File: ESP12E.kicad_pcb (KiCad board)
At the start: 2 copper layers, 40.6 x 41.5 mm, 32 parts, among them J1 Conn_01x06_Pin, J2 Conn_01x06_Pin, P1 USB_C_Plug_USB2.0, Q3 SS8050, Q4 SS8050, U1 ESP-12E, U2 CH340G, U3 AMS1117-3.3, Y1 Crystal_GND23

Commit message: Feat: adding IRF520 mosfets for controlling Motor of air pump and 4 solinoids.
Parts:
- removed C5: 10pF, Capacitor_SMD:C_0201_0603Metric
- removed C6: 10uF, Capacitor_SMD:C_0201_0603Metric
- removed C7: 100nF, Capacitor_SMD:C_0201_0603Metric
- removed P1: USB_C_Plug_USB2.0, Connector_USB:USB_C_Receptacle_GCT_USB4125-xx-x_6P_TopMnt_Horizontal
- removed U2: CH340G, Package_SO:SOIC-16_3.9x9.9mm_P1.27mm
- removed Y1: Crystal_GND23, Crystal:Crystal_SMD_3225-4Pin_3.2x2.5mm
- added D2: LED, LED_SMD:LED_1206_3216Metric, F.Cu at (54.8, 101.0)
- added D3: LED, LED_SMD:LED_1206_3216Metric, F.Cu at (67.8, 101.0)
- added D4: LED, LED_SMD:LED_1206_3216Metric, F.Cu at (80.8, 101.0)
- added D5: LED, LED_SMD:LED_1206_3216Metric, F.Cu at (93.8, 101.0)
- added J3: UART, Connector_JST:JST_XH_B4B-XH-A_1x04_P2.50mm_Vertical, F.Cu at (28.5, 36.2)
- added J4: Motor, TerminalBlock_Phoenix:TerminalBlock_Phoenix_PT-1,5-2-5.0-H_1x02_P5.00mm_Horizontal, F.Cu at (35.0, 113.0)
- added J5: 12v PWR, TerminalBlock_Phoenix:TerminalBlock_Phoenix_PT-1,5-2-5.0-H_1x02_P5.00mm_Horizontal, F.Cu at (110.5, 113.0)
- added J6: Sol_1, TerminalBlock_Phoenix:TerminalBlock_Phoenix_PT-1,5-2-5.0-H_1x02_P5.00mm_Horizontal, F.Cu at (48.0, 113.0)
- added J7: Sol_2, TerminalBlock_Phoenix:TerminalBlock_Phoenix_PT-1,5-2-5.0-H_1x02_P5.00mm_Horizontal, F.Cu at (61.0, 113.0)
- added J8: Sol_3, TerminalBlock_Phoenix:TerminalBlock_Phoenix_PT-1,5-2-5.0-H_1x02_P5.00mm_Horizontal, F.Cu at (74.0, 113.0)
- added J9: Sol_4, TerminalBlock_Phoenix:TerminalBlock_Phoenix_PT-1,5-2-5.0-H_1x02_P5.00mm_Horizontal, F.Cu at (87.0, 113.0)
- added Q1: IRF520N, Package_TO_SOT_THT:TO-220-3_Vertical, F.Cu at (36.0, 103.5)
- added Q2: IRF520N, Package_TO_SOT_THT:TO-220-3_Vertical, F.Cu at (49.0, 103.5)
- added Q5: IRF520N, Package_TO_SOT_THT:TO-220-3_Vertical, F.Cu at (88.0, 103.5)
- added R13: 1k, Resistor_THT:R_Axial_DIN0309_L9.0mm_D3.2mm_P12.70mm_Horizontal, F.Cu at (66.0, 93.7)
- added R14: 1k, Resistor_THT:R_Axial_DIN0309_L9.0mm_D3.2mm_P12.70mm_Horizontal, F.Cu at (74.0, 93.7)
- added R15: 1k, Resistor_THT:R_Axial_DIN0309_L9.0mm_D3.2mm_P12.70mm_Horizontal, F.Cu at (79.0, 93.7)
- added R16: 1k, Resistor_THT:R_Axial_DIN0309_L9.0mm_D3.2mm_P12.70mm_Horizontal, F.Cu at (87.0, 93.7)
- added R17: 1k, Resistor_THT:R_Axial_DIN0309_L9.0mm_D3.2mm_P12.70mm_Horizontal, F.Cu at (92.0, 93.7)
- C1, C4: footprint Capacitor_SMD:C_0201_0603Metric -> Capacitor_THT:C_Disc_D3.0mm_W2.0mm_P2.50mm
- C2, C3: footprint Capacitor_SMD:C_0201_0603Metric -> Capacitor_THT:C_Radial_D5.0mm_H5.0mm_P2.00mm
- D1: value 1N5819WS -> LED; footprint Diode_SMD:D_SOD-323 -> LED_SMD:LED_1206_3216Metric
- Q3, Q4: value SS8050 -> IRF520N; footprint Package_TO_SOT_SMD:SOT-23 -> Package_TO_SOT_THT:TO-220-3_Vertical
- R1: footprint Resistor_SMD:R_0201_0603Metric -> Resistor_THT:R_Axial_DIN0309_L9.0mm_D3.2mm_P12.70mm_Horizontal
- R10, R11: value 470 -> 1k; footprint Resistor_SMD:R_0201_0603Metric -> Resistor_THT:R_Axial_DIN0309_L9.0mm_D3.2mm_P12.70mm_Horizontal
- R12: value 5k1 -> 1k; footprint Resistor_SMD:R_0201_0603Metric -> Resistor_THT:R_Axial_DIN0309_L9.0mm_D3.2mm_P12.70mm_Horizontal
- R2, R3, R4, R5, R6, R7: footprint Resistor_SMD:R_0402_1005Metric -> Resistor_THT:R_Axial_DIN0309_L9.0mm_D3.2mm_P12.70mm_Horizontal
- R8, R9: value 10k -> 1k; footprint Resistor_SMD:R_0201_0603Metric -> Resistor_THT:R_Axial_DIN0309_L9.0mm_D3.2mm_P12.70mm_Horizontal
- moved C2 161.2 mm to (277.0, 122.0), turned to 90 degrees
- moved U3 153.0 mm to (267.5, 113.0)
- moved C3 148.6 mm to (268.0, 122.0)
- moved C4 142.3 mm to (260.5, 122.2)
- moved IO1 112.5 mm to (216.2, 35.2)
- moved J2 112.5 mm to (252.8, 60.5)
- moved R8 102.2 mm to (35.0, 93.7), turned to 90 degrees
- moved C1 102.1 mm to (57.5, 28.2), turned to -90 degrees
- moved R9 99.6 mm to (40.0, 93.7), turned to 90 degrees
- moved R1 88.6 mm to (64.3, 35.0), turned to 180 degrees
- moved R10 87.6 mm to (48.0, 93.7), turned to 90 degrees
- moved RST1 85.7 mm to (63.0, 29.5), turned to 0 degrees
- moved D1 83.6 mm to (41.8, 101.0), turned to 90 degrees
- moved R11 82.2 mm to (53.0, 93.7)
- moved Flash1 81.7 mm to (89.5, 29.5), turned to 180 degrees
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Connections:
- D1 pad 1: +5V -> GND
- Q3 pad 1: Net-(Q3-B) -> GPIO
- Q3 pad 2: Net-(Q3-E) -> Net-(J7-Pin_2)
- Q3 pad 3: RST -> GND
- Q4 pad 1: Net-(Q4-B) -> GPIO
- Q4 pad 2: Net-(Q4-E) -> Net-(J8-Pin_2)
- Q4 pad 3: D3/GPIO0 -> GND
- R10 pad 1: Net-(U2-TXD) -> GND
- R10 pad 2: RX -> GPIO
- R11 pad 2: TX -> GPIO
- R12 pad 1: Net-(P1-CC) -> GND
- R12 pad 2: GND -> GPIO
- R8 pad 1: Net-(Q3-E) -> GND
- R8 pad 2: Net-(Q4-B) -> GPIO
- R9 pad 1: Net-(Q4-E) -> Net-(D1-A)
- R9 pad 2: Net-(Q3-B) -> GPIO
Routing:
- net GND: track 137.3 -> 0.00 mm, vias 2 -> 0
- net +3.3V: track 122.4 -> 0.00 mm, vias 3 -> 0
- net RST: track 76.4 -> 0.00 mm, vias 3 -> 0
- net +5V: track 69.6 -> 0.00 mm, vias 1 -> 0
- net D3/GPIO0: track 69.2 -> 0.00 mm, vias 2 -> 0
- net RX: track 63.8 -> 0.00 mm, vias 1 -> 0
- net TX: track 60.9 -> 0.00 mm, vias 1 -> 0
- net EN: track 54.1 -> 0.00 mm, vias 3 -> 0
- net A0: track 38.8 -> 0.00 mm
- net D8/GPIO15/SS: track 35.4 -> 0.00 mm, vias 1 -> 0
- net SPI_CS0: track 34.4 -> 0.00 mm, vias 1 -> 0
- net D4/GPIO2: track 31.7 -> 0.00 mm, vias 2 -> 0
- net SPI_MISO: track 30.6 -> 0.00 mm, vias 1 -> 0
- net D2/SDA/GPIO4: track 27.0 -> 0.00 mm, vias 2 -> 0
- net Net-(U2-XO): track 26.9 -> 0.00 mm
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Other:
- board size 40.6 x 41.5 mm -> 100 x 100 mm

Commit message: feat: pcb is ok now, next Pressure sensor.
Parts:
- removed IO1: Conn_01x16_Pin, Connector_PinHeader_2.54mm:PinHeader_1x16_P2.54mm_Vertical
- removed J1, J2: Conn_01x06_Pin, Connector_PinHeader_2.54mm:PinHeader_1x06_P2.54mm_Vertical
- added U2: LM7805_TO220, Package_TO_SOT_THT:TO-220-3_Vertical, F.Cu at (109.9, 100.0)
- moved C2 204.3 mm to (81.6, 62.1)
- moved U3 202.2 mm to (72.0, 61.4)
- moved C4 199.4 mm to (72.8, 55.0), turned to 180 degrees
- moved C3 194.6 mm to (81.6, 66.1), turned to -90 degrees
- moved J3 92.4 mm to (120.5, 27.5), turned to -90 degrees
- moved C1 13.5 mm to (44.0, 28.2)
- moved RST1 13.5 mm to (49.5, 29.5)
- moved R1 13.5 mm to (50.9, 35.0)
- moved R2 13.5 mm to (50.9, 47.0)
- moved R6 13.5 mm to (50.9, 43.0)
- moved R7 13.5 mm to (50.9, 39.0)
- moved Flash1 3.00 mm to (92.5, 29.5)
- moved R3 3.00 mm to (90.7, 35.0)
- moved R4 3.00 mm to (90.7, 39.0)
- moved R5 3.00 mm to (90.7, 43.0)
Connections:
- Q1 pad 1: GPIO -> D5/GPIO14/SCLK
- Q2 pad 1: GPIO -> D6/GPIO12/MISO
- Q3 pad 1: GPIO -> D7/GPIO13/MOSI
- Q4 pad 1: GPIO -> D2/SDA/GPIO4
- Q5 pad 1: GPIO -> D1/SCL/GPIO5
- R10 pad 2: GPIO -> D6/GPIO12/MISO
- R11 pad 2: GPIO -> D6/GPIO12/MISO
- R12 pad 2: GPIO -> D7/GPIO13/MOSI
- R13 pad 2: GPIO -> D7/GPIO13/MOSI
- R14 pad 2: GPIO -> D2/SDA/GPIO4
- R15 pad 2: GPIO -> D2/SDA/GPIO4
- R16 pad 2: GPIO -> D1/SCL/GPIO5
- R17 pad 2: GPIO -> D1/SCL/GPIO5
- R8 pad 2: GPIO -> D5/GPIO14/SCLK
- R9 pad 2: GPIO -> D5/GPIO14/SCLK
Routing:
- net GND: track 0.00 -> 357.0 mm
- net +3.3V: track 0.00 -> 191.6 mm
- net +12V: track 0.00 -> 110.0 mm
- net D5/GPIO14/SCLK: track 0.00 -> 87.9 mm
- net D1/SCL/GPIO5: track 0.00 -> 84.3 mm, vias 0 -> 1
- net D2/SDA/GPIO4: track 0.00 -> 81.7 mm, vias 0 -> 1
- net D6/GPIO12/MISO: track 0.00 -> 81.0 mm
- net D7/GPIO13/MOSI: track 0.00 -> 74.8 mm
- net +5V: track 0.00 -> 61.8 mm
- net RX: track 0.00 -> 42.3 mm
- net TX: track 0.00 -> 41.5 mm
- net RST: track 0.00 -> 31.8 mm
- net EN: track 0.00 -> 26.0 mm
- net Net-(U1-ADC): track 0.00 -> 24.3 mm
- net Net-(J7-Pin_2): track 0.00 -> 14.7 mm
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
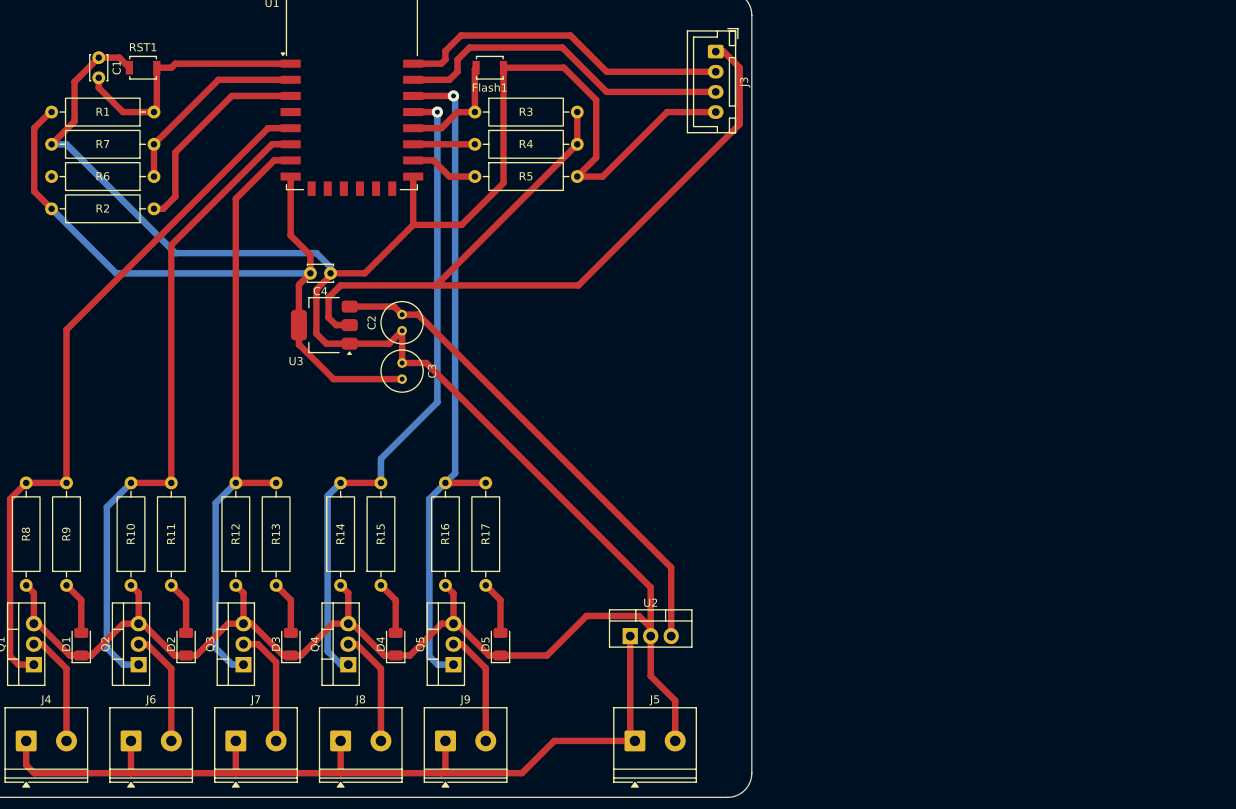
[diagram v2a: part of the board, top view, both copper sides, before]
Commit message: Working: on adding air pressure sensors (MPS-2108).
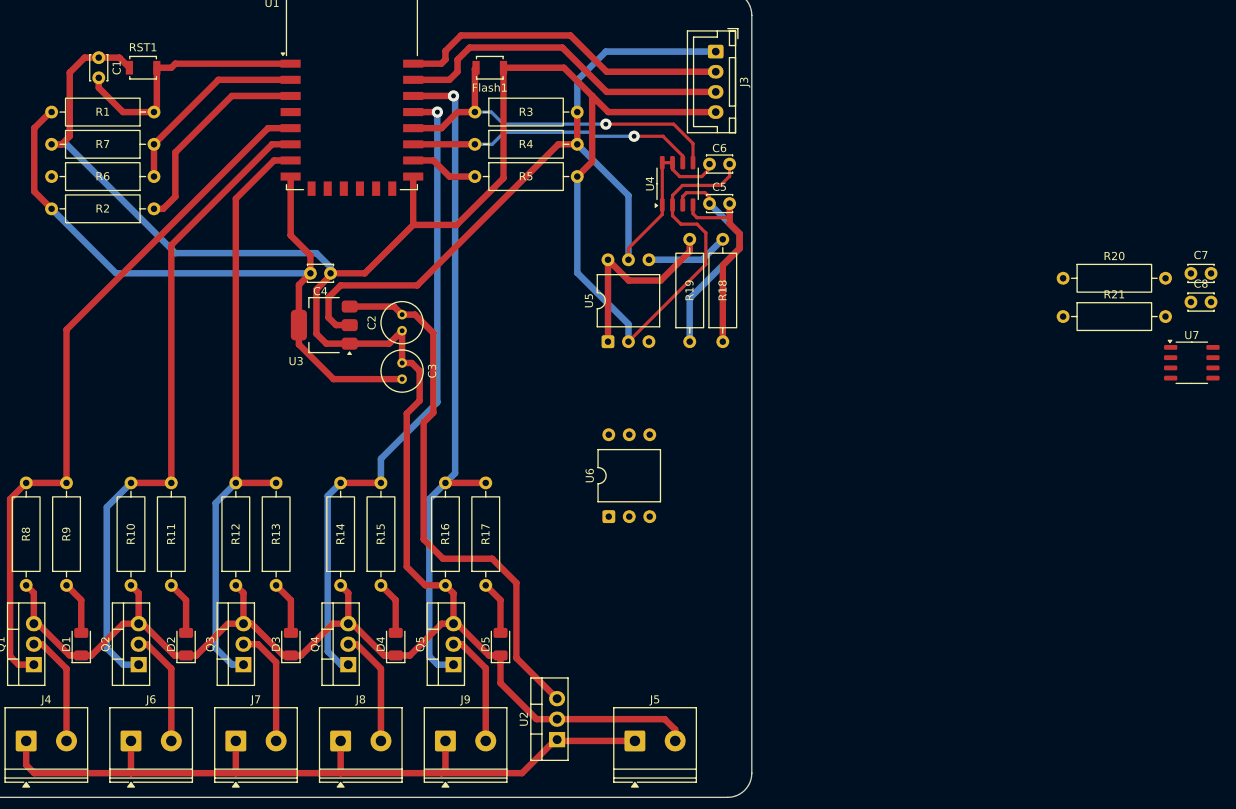
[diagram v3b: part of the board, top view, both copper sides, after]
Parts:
- added C5: 100nF, Capacitor_THT:C_Disc_D3.0mm_W2.0mm_P2.50mm, F.Cu at (119.8, 46.4)
- added C6: 100nF, Capacitor_THT:C_Disc_D3.0mm_W2.0mm_P2.50mm, F.Cu at (119.8, 41.5)
- added C7: 100nF, Capacitor_THT:C_Disc_D3.0mm_W2.0mm_P2.50mm, F.Cu at (179.5, 55.0)
- added C8: 100nF, Capacitor_THT:C_Disc_D3.0mm_W2.0mm_P2.50mm, F.Cu at (179.5, 58.6)
- added R18: 100, Resistor_THT:R_Axial_DIN0309_L9.0mm_D3.2mm_P12.70mm_Horizontal, F.Cu at (121.4, 63.5)
- added R19: 100, Resistor_THT:R_Axial_DIN0309_L9.0mm_D3.2mm_P12.70mm_Horizontal, F.Cu at (117.3, 63.5)
- added R20: 100, Resistor_THT:R_Axial_DIN0309_L9.0mm_D3.2mm_P12.70mm_Horizontal, F.Cu at (163.6, 55.6)
- added R21: 100, Resistor_THT:R_Axial_DIN0309_L9.0mm_D3.2mm_P12.70mm_Horizontal, F.Cu at (163.6, 60.4)
- added U4: HX710(A/B), Package_SO:SOP-8_3.9x4.9mm_P1.27mm, F.Cu at (115.8, 43.9)
- added U5: PSG010R, Package_DIP:DIP-6_W10.16mm, F.Cu at (107.2, 63.5)
- added U6: PSG010R, Package_DIP:DIP-6_W10.16mm, F.Cu at (107.3, 85.2)
- added U7: HX710(A/B), Package_SO:SOP-8_3.9x4.9mm_P1.27mm, F.Cu at (179.6, 66.1)
- moved U2 15.7 mm to (100.8, 112.8), turned to 90 degrees
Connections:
- J3 pad 2: TX -> RX
- J3 pad 3: RX -> TX
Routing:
- net GND: track 357.0 -> 388.8 mm
- net D3/GPIO0: track 14.0 -> 45.1 mm, vias 0 -> 1
- net D4/GPIO2: track 7.65 -> 36.1 mm, vias 0 -> 1
- net Net-(U4-INN): track 0.00 -> 26.8 mm
- net Net-(U4-INP): track 0.00 -> 26.1 mm
- net Net-(R19-Pad2): track 0.00 -> 24.4 mm
- net +12V: track 110.0 -> 96.8 mm
- net Net-(U5-Vo+): track 0.00 -> 10.2 mm
- net +5V: track 61.8 -> 68.0 mm
- net +3.3V: track 191.6 -> 195.9 mm

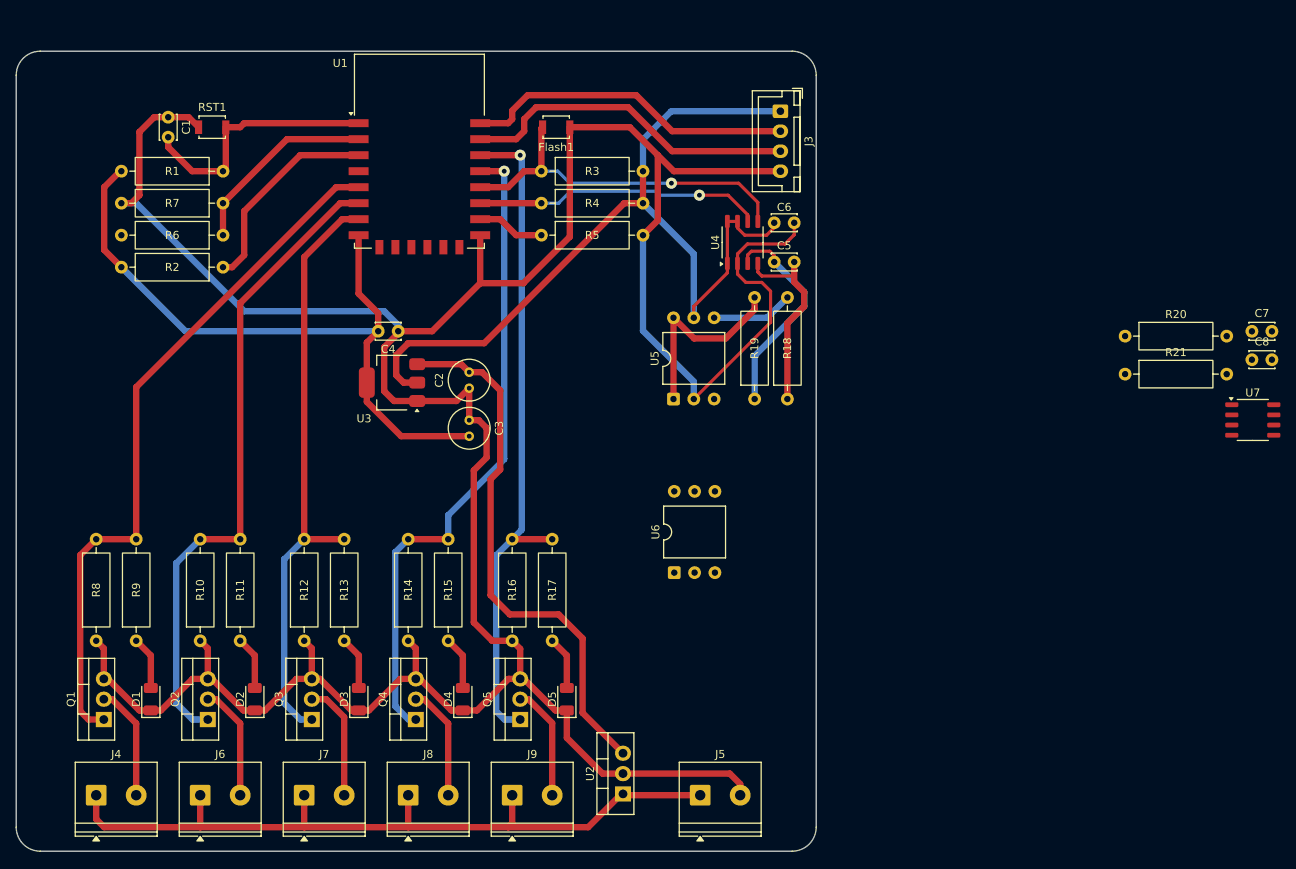
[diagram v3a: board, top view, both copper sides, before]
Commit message: feat: the pressure sensor and some protections (flyback diode) is added.
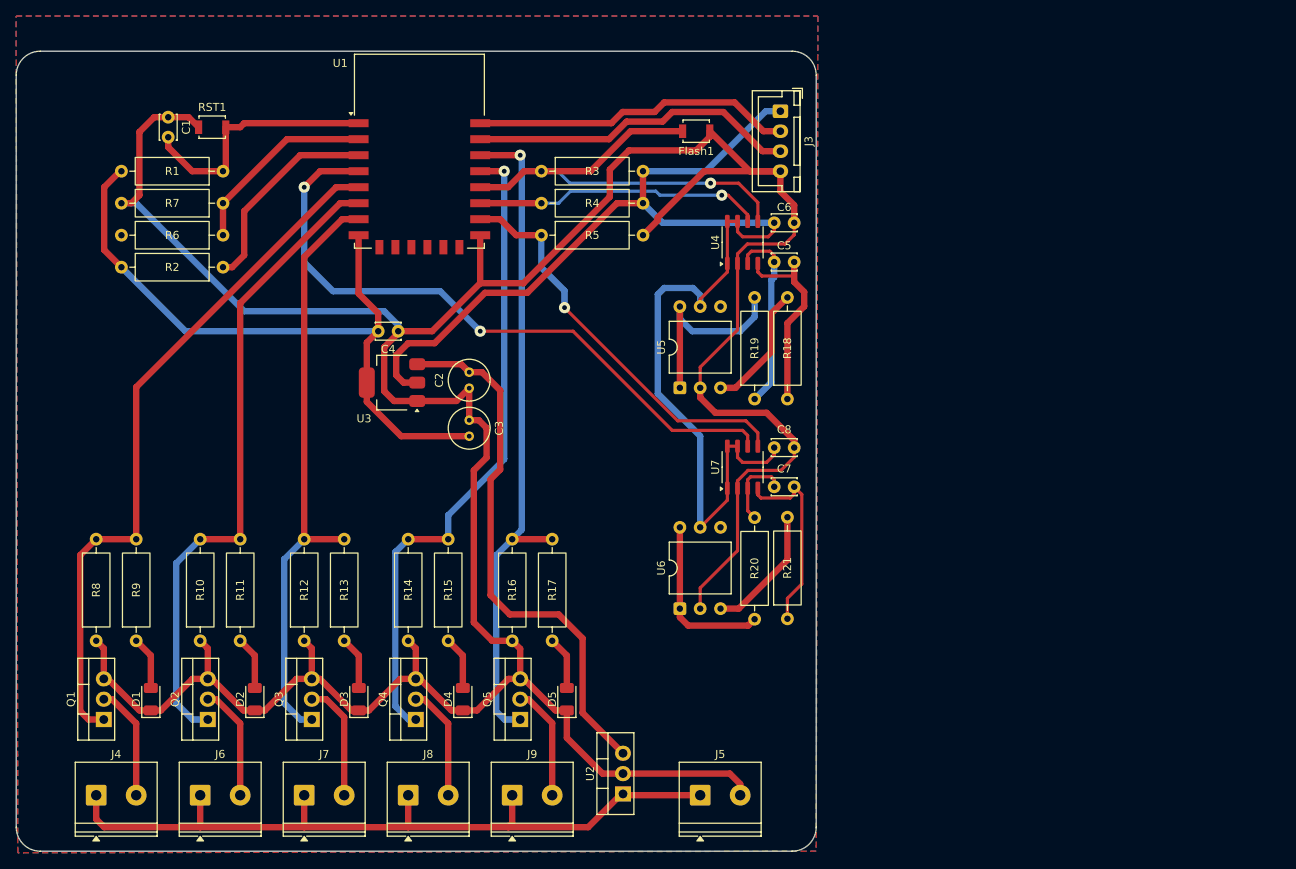
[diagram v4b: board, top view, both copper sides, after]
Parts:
- U5, U6: value PSG010R -> MPS-2108
- moved U7 64.0 mm to (115.8, 72.0), turned to 90 degrees
- moved C7 62.8 mm to (119.8, 74.5)
- moved C8 60.7 mm to (119.8, 69.5)
- moved R21 52.1 mm to (121.4, 91.0), turned to 90 degrees
- moved R20 51.6 mm to (117.3, 78.3), turned to -90 degrees
- moved Flash1 17.5 mm to (110.0, 30.0)
- moved U6 4.55 mm to (108.0, 89.7)
- moved U5 1.61 mm to (108.0, 62.1)
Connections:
- J3 pad 2: RX -> TX
- J3 pad 3: TX -> RX
- U5 pad 3: unconnected-(U5-NC-Pad3) -> Net-(U5-Vo+)
- U5 pad 4: Net-(U5-Vo+) -> unconnected-(U5-NC-Pad4)
- U6 pad 3: unconnected-(U6-NC-Pad3) -> Net-(U6-Vo+)
- U6 pad 4: Net-(U6-Vo+) -> unconnected-(U6-NC-Pad4)
- U7 pad 5: D0/GPIO16 -> D8/GPIO15/SS
- U7 pad 6: D8/GPIO15/SS -> D0/GPIO16
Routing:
- net D0/GPIO16: track 0.00 -> 82.9 mm, vias 0 -> 2
- net +3.3V: track 195.9 -> 252.1 mm
- net D8/GPIO15/SS: track 8.48 -> 51.0 mm, vias 0 -> 1
- net GND: track 388.8 -> 413.9 mm
- net Net-(U7-INP): track 0.00 -> 24.3 mm
- net Net-(R20-Pad2): track 0.00 -> 21.3 mm
- net Net-(U6-Vo+): track 0.00 -> 16.2 mm
- net D3/GPIO0: track 45.1 -> 59.2 mm
- net Net-(U7-INN): track 0.00 -> 9.61 mm
- net Net-(U5-Vo+): track 10.2 -> 15.9 mm
- net Net-(U4-INN): track 26.8 -> 23.7 mm
- net RX: track 42.3 -> 41.0 mm
- net TX: track 41.5 -> 40.1 mm
- added copper zone on B.Cu, net GND
- added copper zone on F.Cu, net GND
